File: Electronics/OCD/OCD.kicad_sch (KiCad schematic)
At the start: 27 parts, among them J1 TE-CK-6.35-29B, J2 Barrel_Jack_Switch, J3 PJ-645C MONO, SW1 SW_3PDT_x3, U1 TL074H, U2 TL074H

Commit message: silkscreen pdf and schematic update to center-negative
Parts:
- BT1: footprint (none) -> Connector_PinHeader_2.54mm:PinHeader_1x02_P2.54mm_Vertical
- C1, C11, C12, C2, C3, C6: footprint (none) -> Capacitor_SMD:C_0805_2012Metric
- J2: footprint (none) -> Connector_PinHeader_2.54mm:PinHeader_1x03_P2.54mm_Vertical
- R1, R16, R17, R18, R19, R2, R20, R21, R22, R3, R4, R5: footprint (none) -> Resistor_SMD:R_0805_2012Metric
- SW1: footprint (none) -> Connector_PinHeader_2.54mm:PinHeader_1x09_P2.54mm_Vertical
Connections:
- net +9V: now also J2.2; no longer BT1.1 (+), J2.1
- net JGND: now also J2.1
- net input_sleeve: now also BT1.2 (-); no longer J2.2
- net at J2.3: now also BT1.1 (+); no longer BT1.2 (-)
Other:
- moved on the sheet: BT1, J2

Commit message: RevA release
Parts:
- added C13: 220uF, Capacitor_SMD:CP_Elec_8x10, symbol Device:C_Polarized_US
- R19: value 47K -> 47k
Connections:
- net +9V: now also C13.1
- net JGND: now also C13.2
- net input_raw: now also SW1.7 (A)
- no-connect marks 5 -> 4
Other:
- note added: "3PDT Switch Wiring"
- note added: "COM"
- note added: "NC"
- note added: "NO"
- note added: "POLE 1"
- note added: "POLE 2"
- note added: "POLE 3"
- moved on the sheet: C11, C12, D1, R1, SW1C, U1E, U2E

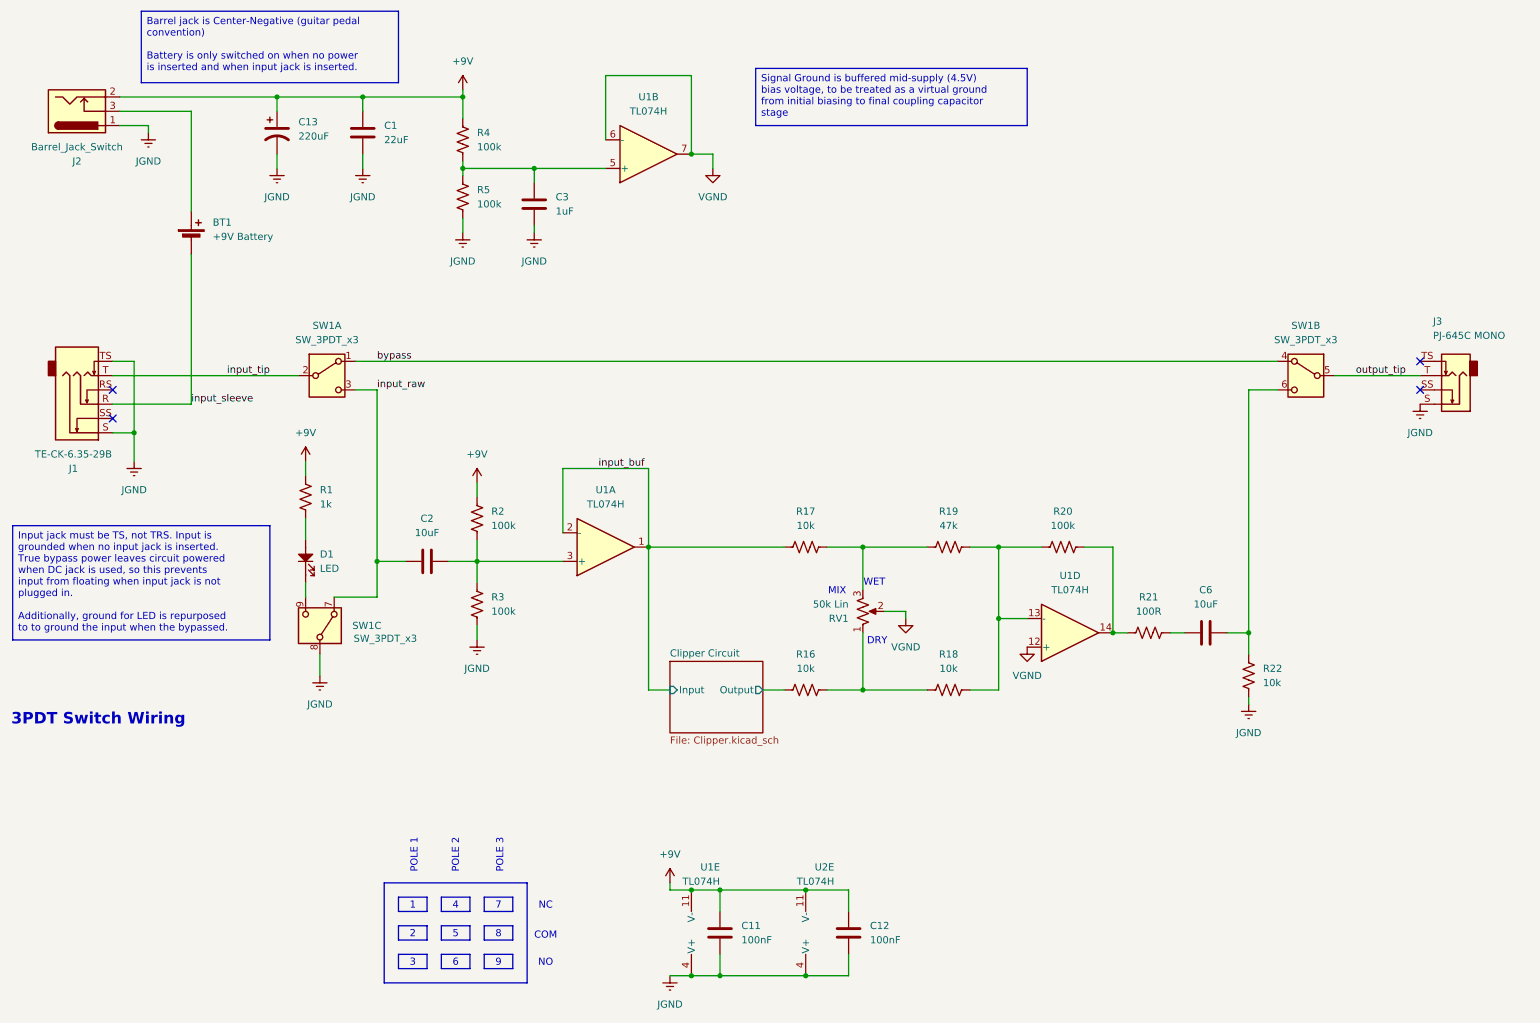
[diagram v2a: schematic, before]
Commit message: RevB release. Corrected opamp orientation, added pad switch
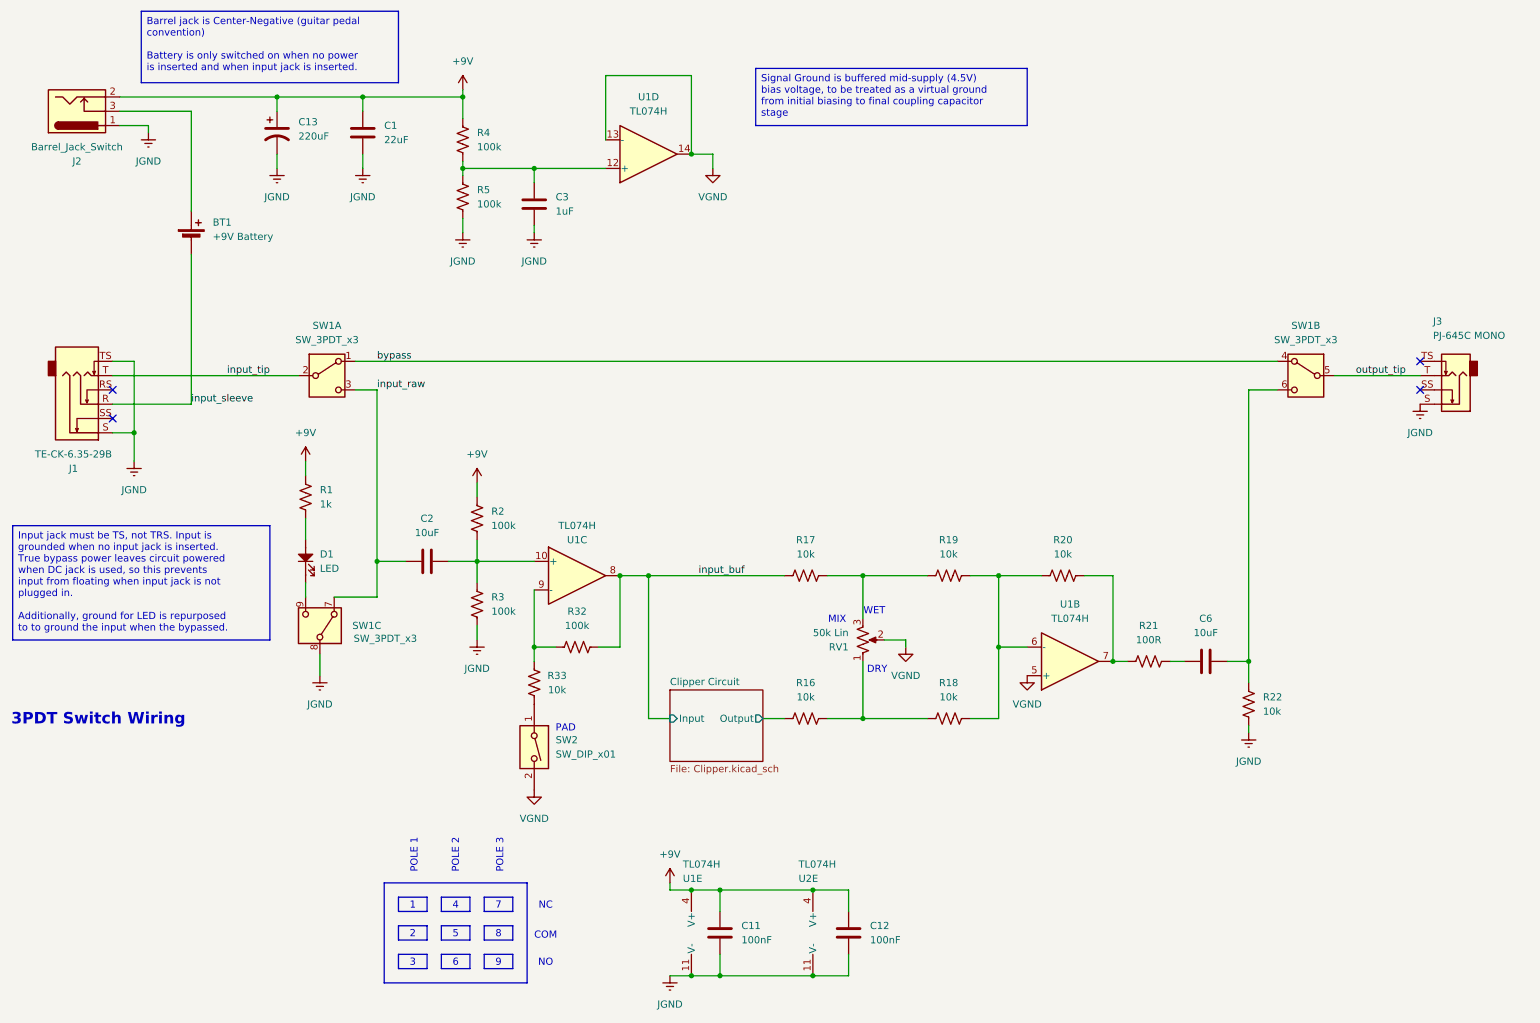
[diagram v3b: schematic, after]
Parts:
- removed unit 1 of U1
- added R32: 100k, Resistor_SMD:R_0805_2012Metric, symbol Device:R_US
- added R33: 10k, Resistor_SMD:R_0805_2012Metric, symbol Device:R_US
- added SW2: SW_DIP_x01, Button_Switch_SMD:SW_DIP_SPSTx01_Slide_6.7x4.1mm_W8.61mm_P2.54mm_LowProfile, symbol Switch:SW_DIP_x01
- added unit 3 of U1
- C1: Distributer (none) -> LCSC; Manufacturer (none) -> Samsung Electro-Mechanics; Part Number (none) -> CL21A226MAQNNNE; SKU (none) -> C45783
- C11, C12: Distributer (none) -> LCSC; Manufacturer (none) -> Samsung Electro-Mechanics; Part Number (none) -> CL21B104KCFNNNE; SKU (none) -> C28233
- C13: Distributer Digi-Key -> LCSC; SKU 493-2278-2-ND -> C433299
- C2, C6: Distributer (none) -> LCSC; Manufacturer (none) -> Murata Electronics; Part Number (none) -> GRM21BZ71E106KE15L; SKU (none) -> C237493
- C3: Distributer (none) -> LCSC; Manufacturer (none) -> Samsung Electro-Mechanics; Part Number (none) -> CL21B105KBFNNNE; SKU (none) -> C28323
- D1: Distributer (none) -> TAYDA; Manufacturer (none) -> PIC; Part Number (none) -> PBS-24-302-N2 Red/Green LED; SKU (none) -> A-1784; now left out of the parts list
- R1: Distributer (none) -> LCSC; Manufacturer (none) -> UNI-ROYAL(Uniroyal Elec); Part Number (none) -> 0805W8F1001T5E; SKU (none) -> C17513
- R16, R17, R18, R22: Distributer (none) -> LCSC; Manufacturer (none) -> UNI-ROYAL(Uniroyal Elec); Part Number (none) -> 0805W8F1002T5E; SKU (none) -> C17414
- R19: value 47k -> 10k; Distributer (none) -> LCSC; Manufacturer (none) -> UNI-ROYAL(Uniroyal Elec); Part Number (none) -> 0805W8F1002T5E; SKU (none) -> C17414
- R2, R3, R4, R5: Distributer (none) -> LCSC; Manufacturer (none) -> UNI-ROYAL(Uniroyal Elec); Part Number (none) -> 0805W8F1003T5E; SKU (none) -> C149504
- R20: value 100k -> 10k; Distributer (none) -> LCSC; Manufacturer (none) -> UNI-ROYAL(Uniroyal Elec); Part Number (none) -> 0805W8F1002T5E; SKU (none) -> C17414
- R21: Distributer (none) -> LCSC; Manufacturer (none) -> UNI-ROYAL(Uniroyal Elec); Part Number (none) -> 0805W8F1000T5E; SKU (none) -> C17408
- SW1: Part Number PBS24302 -> PBS-24-302-N2 Red/Green LED; SKU A-331 -> A-1784
- U1, U2: Distributer (none) -> LCSC; SKU (none) -> C2878713
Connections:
- net +9V: now also U1.4 (V+), U2.4 (V+); no longer U1.11 (V-), U2.11 (V-)
- net JGND: now also U1.11 (V-), U2.11 (V-); no longer U1.4 (V+), U2.4 (V+)
- net VGND: now also U1.13 (-), U1.14, U1.5 (+), SW2.2; no longer U1.12 (+), U1.6 (-), U1.7
- net input_buf: now also R32.2, U1.8
- net at C2.2, R2.2, R3.1: now also U1.10 (+)
- net at R18.2, R19.2, R20.1: now also U1.6 (-); no longer U1.13 (-)
- net at R20.2, R21.1: now also U1.7; no longer U1.14
- net at C3.1, R4.2, R5.1: now also U1.12 (+); no longer U1.5 (+)
- new net: R33.2, SW2.1
- new net: R32.1, R33.1, U1.9 (-)
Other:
- note added: "PAD"
- moved on the sheet: C6, R16, R17, R18, R19, R20, R21, R22, RV1
